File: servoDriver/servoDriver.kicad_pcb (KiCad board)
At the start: 2 copper layers, 25 x 14 mm, 19 parts, among them J1 Conn_01x04_Male, J2 Conn_01x04_Male, J3 Conn_01x03_Male, J4 Conn_01x03_Male, J5 Conn_01x03_Male, J6 SWD, U1 STM32F042F6Px, U2 AP131-33, U3 TCAN330, Y1 8MHz

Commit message: Version 2 PCB?
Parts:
- J6: footprint Connector_PinHeader_1.00mm:PinHeader_1x04_P1.00mm_Vertical -> Connector_PinHeader_1.27mm:PinHeader_1x04_P1.27mm_Vertical
- JP1, JP2: footprint Jumper:SolderJumper-2_P1.3mm_Open_Pad1.0x1.5mm -> servoDriver:SolderJumper-2_P1.3mm_Open_RoundedPad1.0x1.5mm
- moved J6 0.72 mm to (81.5, 64.0)
- moved C5 0.10 mm to (94.2, 63.5)
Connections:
- U1 pad 1: Net-(U1-Pad1) -> /P-
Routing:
- net /P-: track 76.2 -> 79.0 mm
- net /DCLK: track 43.9 -> 46.1 mm, vias 2 -> 3
- net /Comms2: track 45.7 -> 47.8 mm
- net /pwm3: track 29.1 -> 27.5 mm
- net /tx: track 27.2 -> 28.0 mm
- net /DIO: track 30.3 -> 29.9 mm, vias 1 -> 2
- net /3v3: track 48.7 -> 48.3 mm, vias 4 -> 3
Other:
- board size 25 x 14 mm -> 25.4 x 14 mm
- board text added: "GND"

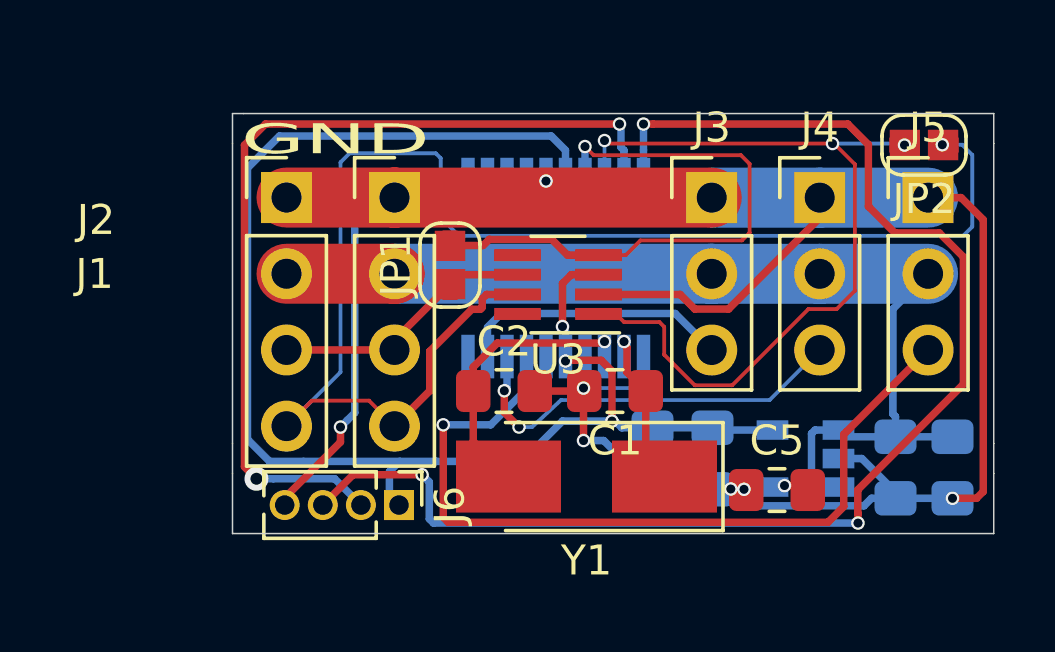
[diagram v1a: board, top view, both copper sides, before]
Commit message: PCB updates  * V3  * Added extra channel  * Using closely spaced pins.
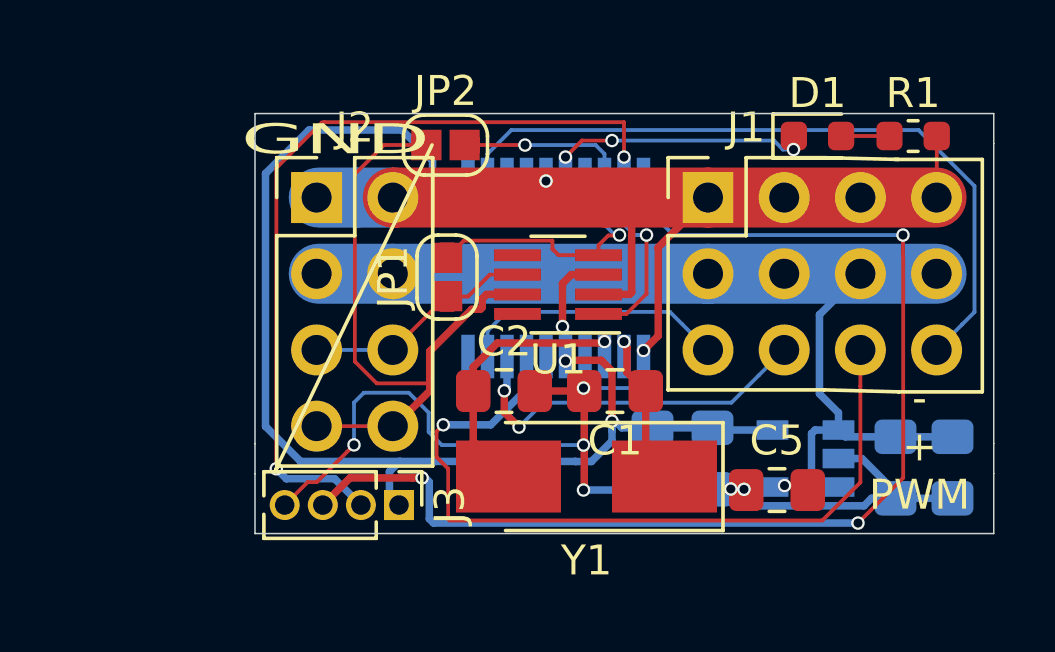
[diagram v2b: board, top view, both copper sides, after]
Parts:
- removed the J3 at (92.0, 53.8)
- removed J4, J5: Conn_01x03_Male, Connector_PinHeader_2.54mm:PinHeader_1x03_P2.54mm_Vertical
- added D1: LED, LED_SMD:LED_0603_1608Metric, F.Cu at (95.5, 51.8)
- added R1: R_Small, Resistor_SMD:R_0603_1608Metric, F.Cu at (98.7, 51.8)
- J1: value Conn_01x04_Male -> Conn_01x12; footprint Connector_PinHeader_2.54mm:PinHeader_1x04_P2.54mm_Vertical -> servoDriver:PinHeader_3x04_P2.54mm_Vertical
- J2: value Conn_01x04_Male -> Conn_02x04_Odd_Even; footprint Connector_PinHeader_2.54mm:PinHeader_1x04_P2.54mm_Vertical -> Connector_PinHeader_2.54mm:PinHeader_2x04_P2.54mm_Vertical
- moved JP2 16.0 mm to (83.1, 52.0), turned to 0 degrees
- moved J1 10.4 mm to (91.8, 53.8)
- moved J2 1.00 mm to (78.8, 53.8)
- moved JP1 0.41 mm to (83.2, 56.5)
- renumbered J6 to J3, U3 to U1, U1 to U2, U2 to U3
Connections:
- J1 pad 3: /Comms1 -> /pwm1
- J1 pad 4: /Comms2 -> /P-
- J2 pad 2: /P+ -> /P-
- J2 pad 3: /Comms1 -> /P+
- J2 pad 4: /Comms2 -> /P+
- U2 pad 12: Net-(U1-Pad12) -> /pwm4
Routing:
- net /Comms2: track 47.8 -> 21.2 mm, vias 1 -> 0
- net /pwm4: track 0.00 -> 24.2 mm
- net /tx: track 28.0 -> 12.7 mm, vias 3 -> 2
- net /rx: track 19.6 -> 9.66 mm
- net /3v3: track 48.3 -> 57.8 mm, vias 3 -> 6
- net /P-: track 79.0 -> 71.4 mm, vias 7 -> 8
- net /DCLK: track 46.1 -> 40.4 mm
- net /DIO: track 29.9 -> 27.5 mm
- net Net-(D1-Pad2): track 0.00 -> 1.61 mm
- net /pwm2: track 13.7 -> 12.5 mm
- net /pwm3: track 27.5 -> 26.5 mm
- net /Comms1: track 8.93 -> 8.07 mm
- net /P+: track 34.8 -> 34.1 mm
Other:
- board size 25.4 x 14 mm -> 24.6 x 14 mm
- board text added: "- + PWM"

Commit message: Version 3
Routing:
- net /P-: vias 8 -> 7
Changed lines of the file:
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@@
     (thickness 1.6)
     (drawings 16)
-    (tracks 269)
+    (tracks 268)
     (zones 0)
     (modules 18)
@@
       (drillshape 0)
       (scaleselection 1)
-      (outputdirectory "v2/"))
+      (outputdirectory "v3/"))
   )
   (net 0 "")
@@
   (via (at 87.7 62.05) (size 0.45) (drill 0.3) (layers F.Cu B.Cu) (net 4))
   (via (at 89.7 58.9) (size 0.45) (drill 0.3) (layers F.Cu B.Cu) (net 4))
-  (via (at 92.61 63.515) (size 0.45) (drill 0.3) (layers F.Cu B.Cu) (net 4))
   (via (at 87.7 60.15) (size 0.45) (drill 0.3) (layers F.Cu B.Cu) (net 4))
   (via (at 86.45 53.25) (size 0.45) (drill 0.3) (layers F.Cu B.Cu) (net 4))
